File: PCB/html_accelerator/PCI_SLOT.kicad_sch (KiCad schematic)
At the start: 13 parts, among them J1 Bus_PCI_Express_x16, J3 PCIexpress_bracket, U1 MCS9990

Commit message: layout and 3d updates
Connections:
- net 50_PCIE_TXC_N: now reaches C2.2, U1.14 (PCIE_TXDN)
- net 50_PCIE_CLK_P: now reaches J1.A13 (REFCLK+), U1.5 (PCIE_REFCLKP)
- net 50_PCIE_CLK_N: now reaches J1.A14 (REFCLK-), U1.4 (PCIE_REFCLKN)
- net 50_PCIE_TXC_P: now reaches C1.2, U1.13 (PCIE_TXDP)
- net PCIE_RXn renamed 50_PCIE_RX_N
- net PCIE_RXp renamed 50_PCIE_RX_P
- net PCIE_TXn renamed 50_PCIE_TX_N
- net PCIE_TXp renamed 50_PCIE_TX_P
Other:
- moved on the sheet: C1, C2
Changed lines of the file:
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@@
+    (stroke (width 0) (type default))
+  )
+  (wire (pts (xy 17.78 72.39) (xy 30.48 72.39))
     (stroke (width 0) (type default))
   )
@@
     (stroke (width 0) (type default))
   )
+  (wire (pts (xy 121.92 105.41) (xy 137.16 105.41))
+    (stroke (width 0) (type default))
+  )
   (wire (pts (xy 168.91 158.75) (xy 167.64 158.75))
     (stroke (width 0) (type default))
   )
+  (wire (pts (xy 38.1 77.47) (xy 53.34 77.47))
+    (stroke (width 0) (type default))
+  )
   (wire (pts (xy 168.91 168.91) (xy 167.64 168.91))
     (stroke (width 0) (type default))
@@
     (stroke (width 0) (type default))
   )
-  (wire (pts (xy 52.07 90.17) (xy 53.34 90.17))
+  (wire (pts (xy 41.91 90.17) (xy 53.34 90.17))
     (stroke (width 0) (type default))
   )
@@
     (stroke (width 0) (type default))
   )
-  (wire (pts (xy 52.07 86.36) (xy 52.07 85.09))
+  (wire (pts (xy 41.91 86.36) (xy 41.91 85.09))
     (stroke (width 0) (type default))
   )
@@
     (stroke (width 0) (type default))
   )
-  (wire (pts (xy 27.94 78.74) (xy 38.1 78.74))
-    (stroke (width 0) (type default))
-  )
   (wire (pts (xy 135.89 179.07) (xy 137.16 179.07))
     (stroke (width 0) (type default))
   )
-  (wire (pts (xy 45.72 78.74) (xy 46.99 78.74))
-    (stroke (width 0) (type default))
-  )
-  (wire (pts (xy 52.07 88.9) (xy 52.07 90.17))
-    (stroke (width 0) (type default))
-  )
-  (wire (pts (xy 124.46 102.87) (xy 137.16 102.87))
+  (wire (pts (xy 41.91 88.9) (xy 41.91 90.17))
+    (stroke (width 0) (type default))
+  )
+  (wire (pts (xy 121.92 102.87) (xy 137.16 102.87))
     (stroke (width 0) (type default))
   )
@@
     (stroke (width 0) (type default))
   )
-  (wire (pts (xy 52.07 85.09) (xy 53.34 85.09))
+  (wire (pts (xy 41.91 85.09) (xy 53.34 85.09))
     (stroke (width 0) (type default))
   )
@@
     (stroke (width 0) (type default))
   )
-  (wire (pts (xy 46.99 77.47) (xy 53.34 77.47))
-    (stroke (width 0) (type default))
-  )
   (wire (pts (xy 135.89 118.11) (xy 137.16 118.11))
     (stroke (width 0) (type default))
@@
     (stroke (width 0) (type default))
   )
-  (wire (pts (xy 46.99 78.74) (xy 46.99 77.47))
-    (stroke (width 0) (type default))
-  )
   (wire (pts (xy 91.44 96.52) (xy 95.25 96.52))
     (stroke (width 0) (type default))
@@
     (stroke (width 0) (type default))
   )
+  (wire (pts (xy 17.78 77.47) (xy 30.48 77.47))
+    (stroke (width 0) (type default))
+  )
   (wire (pts (xy 132.08 57.15) (xy 125.73 57.15))
     (stroke (width 0) (type default))
@@
     (stroke (width 0) (type default))
   )
-  (wire (pts (xy 27.94 86.36) (xy 52.07 86.36))
+  (wire (pts (xy 17.78 86.36) (xy 41.91 86.36))
     (stroke (width 0) (type default))
   )
@@
     (stroke (width 0) (type default))
   )
-  (wire (pts (xy 46.99 71.12) (xy 46.99 72.39))
-    (stroke (width 0) (type default))
-  )
   (wire (pts (xy 111.76 55.88) (xy 111.76 60.96))
     (stroke (width 0) (type default))
@@
     (stroke (width 0) (type default))
   )
-  (wire (pts (xy 167.64 102.87) (xy 180.34 102.87))
+  (wire (pts (xy 167.64 102.87) (xy 182.88 102.87))
     (stroke (width 0) (type default))
   )
@@
     (stroke (width 0) (type default))
   )
-  (wire (pts (xy 167.64 105.41) (xy 180.34 105.41))
+  (wire (pts (xy 167.64 105.41) (xy 182.88 105.41))
     (stroke (width 0) (type default))
   )
@@
     (stroke (width 0) (type default))
   )
-  (wire (pts (xy 45.72 71.12) (xy 46.99 71.12))
-    (stroke (width 0) (type default))
-  )
   (wire (pts (xy 135.89 115.57) (xy 137.16 115.57))
     (stroke (width 0) (type default))
@@
     (stroke (width 0) (type default))
   )
-  (wire (pts (xy 124.46 105.41) (xy 137.16 105.41))
-    (stroke (width 0) (type default))
-  )
-  (wire (pts (xy 27.94 88.9) (xy 52.07 88.9))
+  (wire (pts (xy 38.1 72.39) (xy 53.34 72.39))
+    (stroke (width 0) (type default))
+  )
+  (wire (pts (xy 17.78 88.9) (xy 41.91 88.9))
     (stroke (width 0) (type default))
   )
@@
     (stroke (width 0) (type default))
   )
-  (wire (pts (xy 27.94 71.12) (xy 38.1 71.12))
-    (stroke (width 0) (type default))
-  )
   (wire (pts (xy 135.89 123.19) (xy 137.16 123.19))
     (stroke (width 0) (type default))
@@
   )
   (wire (pts (xy 91.44 90.17) (xy 106.68 90.17))
-    (stroke (width 0) (type default))
-  )
-  (wire (pts (xy 46.99 72.39) (xy 53.34 72.39))
     (stroke (width 0) (type default))
   )
@@
     (effects (font (size 1.27 1.27)) (justify left bottom))
   )
-  (label "PCIE_RXp" (at 124.46 102.87 0) (fields_autoplaced)
+  (label "50_PCIE_TXC_N" (at 39.37 77.47 0) (fields_autoplaced)
+    (effects (font (size 1.27 1.27)) (justify left bottom))
+  )
+  (label "50_PCIE_RX_P" (at 121.92 102.87 0) (fields_autoplaced)
     (effects (font (size 1.27 1.27)) (justify left bottom))
   )
@@
     (effects (font (size 1.27 1.27)) (justify right bottom))
   )
-  (label "PCIE_TXp" (at 180.34 102.87 180) (fields_autoplaced)
+  (label "50_PCIE_TX_P" (at 182.88 102.87 180) (fields_autoplaced)
     (effects (font (size 1.27 1.27)) (justify right bottom))
   )
-  (label "PCIE_TXp" (at 27.94 71.12 0) (fields_autoplaced)
+  (label "50_PCIE_TX_P" (at 17.78 72.39 0) (fields_autoplaced)
     (effects (font (size 1.27 1.27)) (justify left bottom))
   )
-  (label "PCIE_TXn" (at 27.94 78.74 0) (fields_autoplaced)
+  (label "50_PCIE_CLK_N" (at 92.71 82.55 0) (fields_autoplaced)
+    (effects (font (size 1.27 1.27)) (justify left bottom))
+  )
+  (label "50_PCIE_TX_N" (at 17.78 77.47 0) (fields_autoplaced)
     (effects (font (size 1.27 1.27)) (justify left bottom))
   )
@@
     (effects (font (size 1.27 1.27)) (justify right bottom))
   )
-  (label "PCIE_RXp" (at 27.94 86.36 0) (fields_autoplaced)
+  (label "50_PCIE_RX_P" (at 17.78 86.36 0) (fields_autoplaced)
     (effects (font (size 1.27 1.27)) (justify left bottom))
   )
-  (label "PCIE_TXn" (at 180.34 105.41 180) (fields_autoplaced)
+  (label "50_PCIE_TX_N" (at 182.88 105.41 180) (fields_autoplaced)
     (effects (font (size 1.27 1.27)) (justify right bottom))
   )
-  (label "PCIE_RXn" (at 124.46 105.41 0) (fields_autoplaced)
+  (label "50_PCIE_CLK_P" (at 92.71 80.01 0) (fields_autoplaced)
+    (effects (font (size 1.27 1.27)) (justify left bottom))
+  )
+  (label "50_PCIE_RX_N" (at 121.92 105.41 0) (fields_autoplaced)
     (effects (font (size 1.27 1.27)) (justify left bottom))
   )
@@
     (effects (font (size 1.27 1.27)) (justify right bottom))
   )
-  (label "PCIE_RXn" (at 27.94 88.9 0) (fields_autoplaced)
+  (label "50_PCIE_RX_N" (at 17.78 88.9 0) (fields_autoplaced)
     (effects (font (size 1.27 1.27)) (justify left bottom))
   )
@@
   (label "PeRST" (at 208.28 82.55 180) (fields_autoplaced)
     (effects (font (size 1.27 1.27)) (justify right bottom))
+  )
+  (label "50_PCIE_TXC_P" (at 39.37 72.39 0) (fields_autoplaced)
+    (effects (font (size 1.27 1.27)) (justify left bottom))
   )
   (symbol (lib_id "Device:R_US") (at 129.54 90.17 90) (unit 1)
@@
     )
   )
-  (symbol (lib_id "Device:C") (at 41.91 78.74 90) (mirror x) (unit 1)
+  (symbol (lib_id "Device:C") (at 34.29 77.47 90) (mirror x) (unit 1)
     (in_bom yes) (on_board yes) (dnp no)
-    (property "Reference" "C2" (at 41.91 83.9089 90)
-      (effects (font (size 1.27 1.27)))
-    )
-    (property "Value" "0.1uF" (at 41.91 81.9879 90)
-      (effects (font (size 1.27 1.27)))
-    )
-    (property "Footprint" "Capacitor_SMD:C_0805_2012Metric_Pad1.18x1.45mm_HandSolder" (at 45.72 79.7052 0)
-      (effects (font (size 1.27 1.27)) hide)
-    )
-    (property "Datasheet" "~" (at 41.91 78.74 0)
+    (property "Reference" "C2" (at 34.29 82.6389 90)
+      (effects (font (size 1.27 1.27)))
+    )
+    (property "Value" "0.1uF" (at 34.29 80.7179 90)
+      (effects (font (size 1.27 1.27)))
+    )
+    (property "Footprint" "Capacitor_SMD:C_0805_2012Metric_Pad1.18x1.45mm_HandSolder" (at 38.1 78.4352 0)
+      (effects (font (size 1.27 1.27)) hide)
+    )
+    (property "Datasheet" "~" (at 34.29 77.47 0)
       (effects (font (size 1.27 1.27)) hide)
     )
@@
     )
   )
-  (symbol (lib_id "Device:C") (at 41.91 71.12 90) (unit 1)
-    (in_bom yes) (on_board yes) (dnp no) (fields_autoplaced)
-    (property "Reference" "C1" (at 41.91 65.9511 90)
-      (effects (font (size 1.27 1.27)))
-    )
-    (property "Value" "0.1uF" (at 41.91 67.8721 90)
-      (effects (font (size 1.27 1.27)))
-    )
-    (property "Footprint" "Capacitor_SMD:C_0805_2012Metric_Pad1.18x1.45mm_HandSolder" (at 45.72 70.1548 0)
-      (effects (font (size 1.27 1.27)) hide)
-    )
-    (property "Datasheet" "~" (at 41.91 71.12 0)
-      (effects (font (size 1.27 1.27)) hide)
-    )
+  (symbol (lib_id "Device:C") (at 34.29 72.39 90) (unit 1)
+    (in_bom yes) (on_board yes) (dnp no) (fields_autoplaced)
+    (property "Reference" "C1" (at 34.29 67.2211 90)
+      (effects (font (size 1.27 1.27)))
+    )
+    (property "Value" "0.1uF" (at 34.29 69.1421 90)
+      (effects (font (size 1.27 1.27)))
+    )
+    (property "Footprint" "Capacitor_SMD:C_0805_2012Metric_Pad1.18x1.45mm_HandSolder" (at 38.1 71.4248 0)
+      (effects (font (size 1.27 1.27)) hide)
+    )
+    (property "Datasheet" "~" (at 34.29 72.39 0)
+      (effects (font (size 1.27 1.27)) hide)
+    )

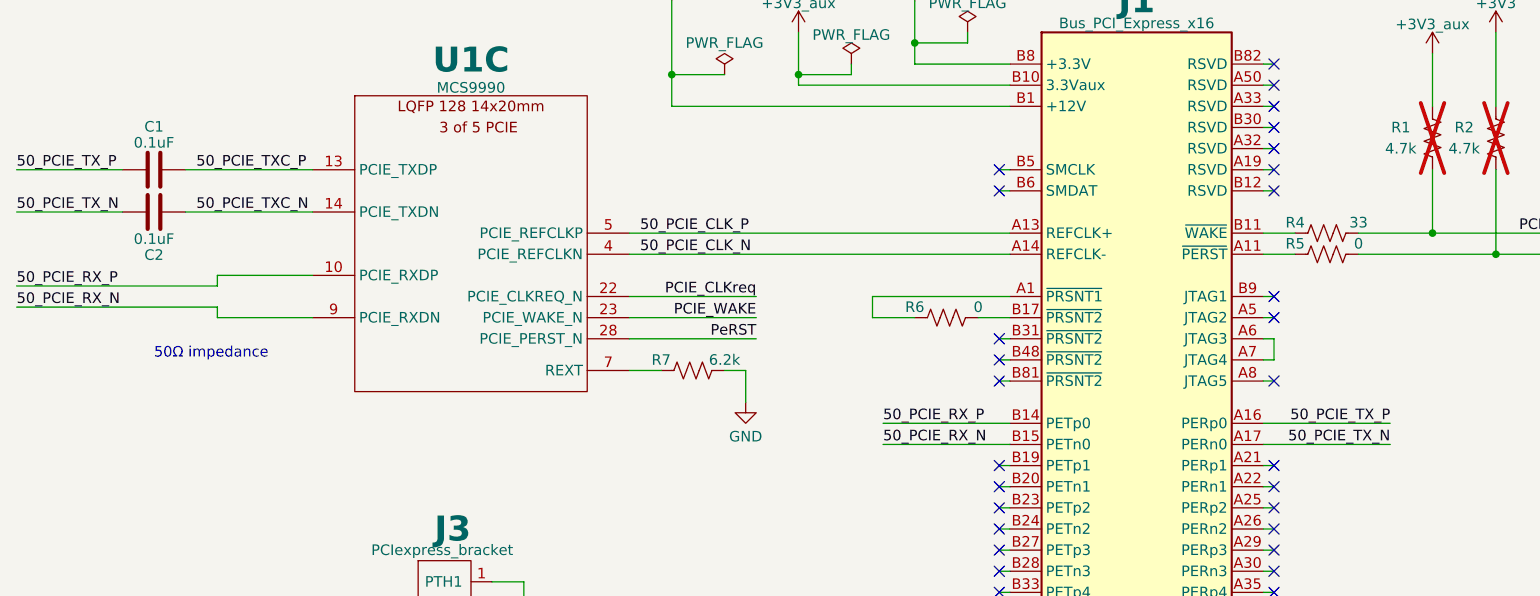
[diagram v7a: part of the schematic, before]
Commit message: impedance controlled nets
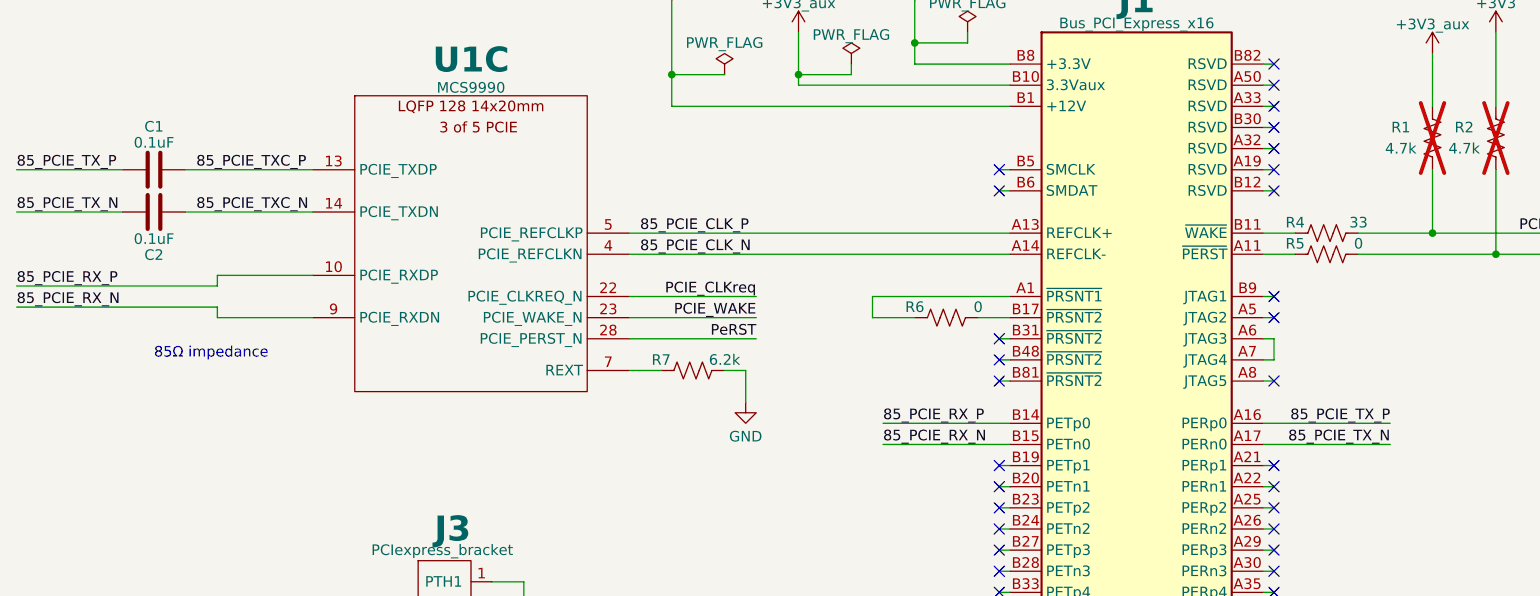
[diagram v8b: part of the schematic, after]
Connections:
- net 50_PCIE_CLK_N renamed 85_PCIE_CLK_N
- net 50_PCIE_CLK_P renamed 85_PCIE_CLK_P
- net 50_PCIE_RX_N renamed 85_PCIE_RX_N
- net 50_PCIE_RX_P renamed 85_PCIE_RX_P
- net 50_PCIE_TXC_N renamed 85_PCIE_TXC_N
- net 50_PCIE_TXC_P renamed 85_PCIE_TXC_P
- net 50_PCIE_TX_N renamed 85_PCIE_TX_N
- net 50_PCIE_TX_P renamed 85_PCIE_TX_P
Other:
- note added: "85Ω impedance"
- note removed: "50Ω impedance"
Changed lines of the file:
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@@
     (stroke (width 0) (type default))
   )
-  (text "50Ω impedance" (at 34.29 95.25 0)
+  (text "85Ω impedance" (at 34.29 95.25 0)
     (effects (font (size 1.27 1.27)) (justify left bottom))
   )
-  (label "50_PCIE_TXC_N" (at 39.37 77.47 0) (fields_autoplaced)
+  (label "85_PCIE_TXC_N" (at 39.37 77.47 0) (fields_autoplaced)
     (effects (font (size 1.27 1.27)) (justify left bottom))
   )
-  (label "50_PCIE_RX_P" (at 121.92 102.87 0) (fields_autoplaced)
+  (label "85_PCIE_RX_P" (at 121.92 102.87 0) (fields_autoplaced)
     (effects (font (size 1.27 1.27)) (justify left bottom))
   )
@@
     (effects (font (size 1.27 1.27)) (justify right bottom))
   )
-  (label "50_PCIE_TX_P" (at 182.88 102.87 180) (fields_autoplaced)
+  (label "85_PCIE_TX_P" (at 182.88 102.87 180) (fields_autoplaced)
     (effects (font (size 1.27 1.27)) (justify right bottom))
   )
-  (label "50_PCIE_TX_P" (at 17.78 72.39 0) (fields_autoplaced)
+  (label "85_PCIE_TX_P" (at 17.78 72.39 0) (fields_autoplaced)
     (effects (font (size 1.27 1.27)) (justify left bottom))
   )
-  (label "50_PCIE_CLK_N" (at 92.71 82.55 0) (fields_autoplaced)
+  (label "85_PCIE_CLK_N" (at 92.71 82.55 0) (fields_autoplaced)
     (effects (font (size 1.27 1.27)) (justify left bottom))
   )
-  (label "50_PCIE_TX_N" (at 17.78 77.47 0) (fields_autoplaced)
+  (label "85_PCIE_TX_N" (at 17.78 77.47 0) (fields_autoplaced)
     (effects (font (size 1.27 1.27)) (justify left bottom))
   )
@@
     (effects (font (size 1.27 1.27)) (justify right bottom))
   )
-  (label "50_PCIE_RX_P" (at 17.78 86.36 0) (fields_autoplaced)
+  (label "85_PCIE_RX_P" (at 17.78 86.36 0) (fields_autoplaced)
     (effects (font (size 1.27 1.27)) (justify left bottom))
   )
-  (label "50_PCIE_TX_N" (at 182.88 105.41 180) (fields_autoplaced)
+  (label "85_PCIE_TX_N" (at 182.88 105.41 180) (fields_autoplaced)
     (effects (font (size 1.27 1.27)) (justify right bottom))
   )
-  (label "50_PCIE_CLK_P" (at 92.71 80.01 0) (fields_autoplaced)
+  (label "85_PCIE_CLK_P" (at 92.71 80.01 0) (fields_autoplaced)
     (effects (font (size 1.27 1.27)) (justify left bottom))
   )
-  (label "50_PCIE_RX_N" (at 121.92 105.41 0) (fields_autoplaced)
+  (label "85_PCIE_RX_N" (at 121.92 105.41 0) (fields_autoplaced)
     (effects (font (size 1.27 1.27)) (justify left bottom))
   )
@@
     (effects (font (size 1.27 1.27)) (justify right bottom))
   )
-  (label "50_PCIE_RX_N" (at 17.78 88.9 0) (fields_autoplaced)
+  (label "85_PCIE_RX_N" (at 17.78 88.9 0) (fields_autoplaced)
     (effects (font (size 1.27 1.27)) (justify left bottom))
   )
@@
     (effects (font (size 1.27 1.27)) (justify right bottom))
   )
-  (label "50_PCIE_TXC_P" (at 39.37 72.39 0) (fields_autoplaced)
+  (label "85_PCIE_TXC_P" (at 39.37 72.39 0) (fields_autoplaced)
     (effects (font (size 1.27 1.27)) (justify left bottom))
   )
